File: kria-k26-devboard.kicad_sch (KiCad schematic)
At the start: 6 parts

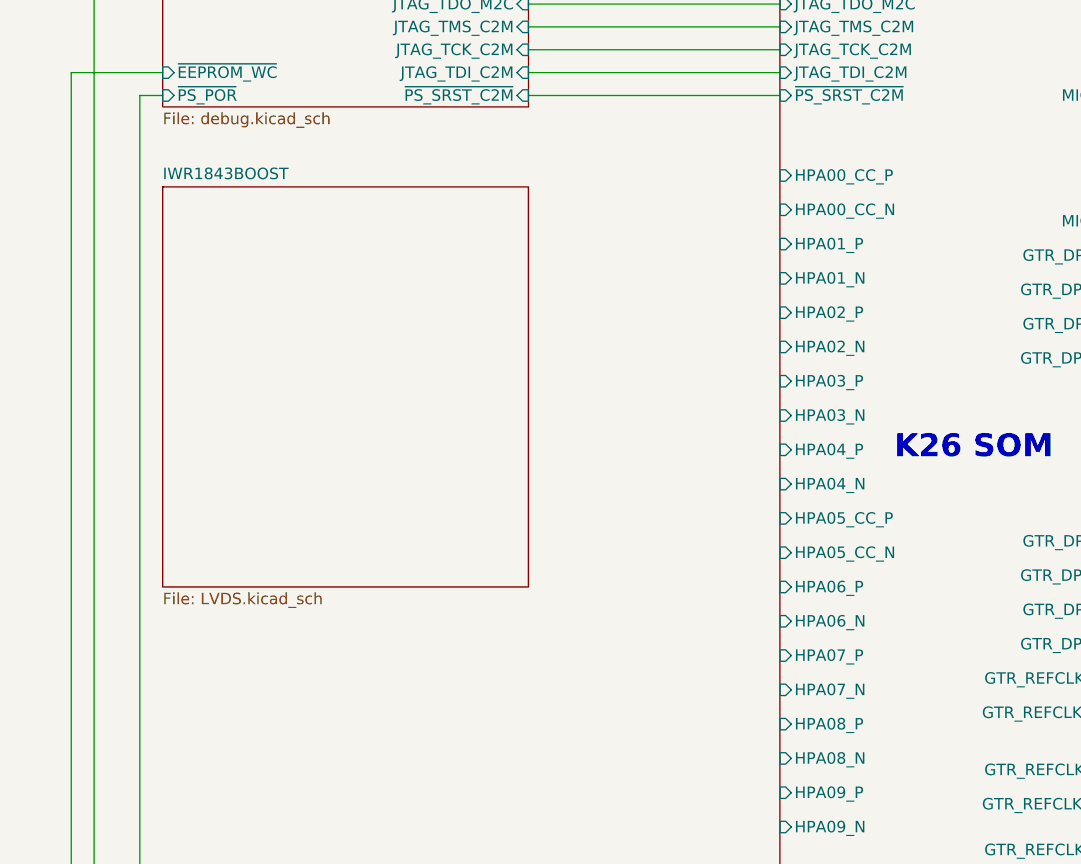
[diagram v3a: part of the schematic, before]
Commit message: Added all components and finished first attempt at schematic
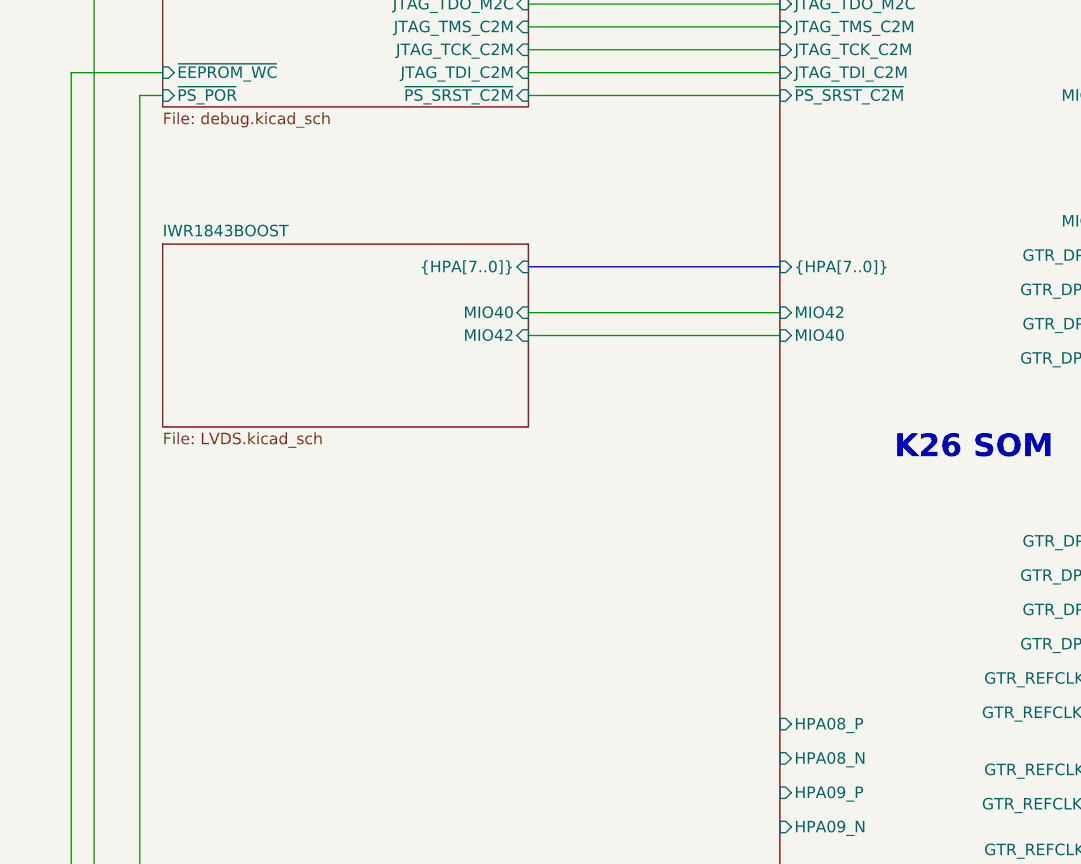
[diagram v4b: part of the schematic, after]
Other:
- sheet IWR1843BOOST ports: added MIO40, MIO42, {HPA[7..0]}; removed none
- sheet Xilinx K26 SOM ports: added MIO40, MIO42, {HPA[7..0]}; removed HPA00_CC_N, HPA00_CC_P, HPA01_N, HPA01_P, HPA02_N, HPA02_P, HPA03_N, HPA03_P, HPA04_N, HPA04_P, HPA05_CC_N, HPA05_CC_P, HPA06_N, HPA06_P, HPA07_N, HPA07_P
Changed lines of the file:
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@@
 		(comment 2 "Antmicro Ltd.")
 	)
+	(bus_alias "HPA[7..0]"
+		(members "HPA01_P" "HPA01_N" "HPA02_P" "HPA02_N" "HPA03_P" "HPA03_N" "HPA04_P"
+			"HPA04_N" "HPA00_CC_P" "HPA00_CC_N" "HPA05_CC_P" "HPA05_CC_N" "HPA06_P"
+			"HPA06_N" "HPA07_P" "HPA07_N"
+		)
+	)
 	(text "Logos"
 		(exclude_from_sim no)
@@
 		)
 	)
+	(wire
+		(pts
+			(xy 151.13 104.14) (xy 179.07 104.14)
+		)
+		(stroke
+			(width 0)
+			(type default)
+		)
+	)
 	(bus
 		(pts
@@
 		)
 	)
+	(bus
+		(pts
+			(xy 151.13 99.06) (xy 179.07 99.06)
+		)
+		(stroke
+			(width 0)
+			(type default)
+		)
+	)
 	(wire
 		(pts
@@
 	(wire
 		(pts
+			(xy 151.13 106.68) (xy 179.07 106.68)
+		)
+		(stroke
+			(width 0)
+			(type default)
+		)
+	)
+	(wire
+		(pts
 			(xy 233.68 184.15) (xy 248.92 184.15)
 		)
@@
 			)
 		)
-		(pin "HPA00_CC_P" input
-			(at 179.07 88.9 180)
-			(effects
-				(font
-					(size 1.27 1.27)
-				)
-				(justify left)
-			)
-		)
-		(pin "HPA00_CC_N" input
-			(at 179.07 92.71 180)
-			(effects
-				(font
-					(size 1.27 1.27)
-				)
-				(justify left)
-			)
-		)
-		(pin "HPA03_P" input
-			(at 179.07 111.76 180)
-			(effects
-				(font
-					(size 1.27 1.27)
-				)
-				(justify left)
-			)
-		)
-		(pin "HPA03_N" input
-			(at 179.07 115.57 180)
-			(effects
-				(font
-					(size 1.27 1.27)
-				)
-				(justify left)
-			)
-		)
 		(pin "HPA08_P" input
 			(at 179.07 149.86 180)
@@
 			)
 		)
-		(pin "HPA02_P" input
-			(at 179.07 104.14 180)
-			(effects
-				(font
-					(size 1.27 1.27)
-				)
-				(justify left)
-			)
-		)
-		(pin "HPA02_N" input
-			(at 179.07 107.95 180)
-			(effects
-				(font
-					(size 1.27 1.27)
-				)
-				(justify left)
-			)
-		)
-		(pin "HPA01_P" input
-			(at 179.07 96.52 180)
-			(effects
-				(font
-					(size 1.27 1.27)
-				)
-				(justify left)
-			)
-		)
-		(pin "HPA01_N" input
-			(at 179.07 100.33 180)
-			(effects
-				(font
-					(size 1.27 1.27)
-				)
-				(justify left)
-			)
-		)
 		(pin "HPA09_P" input
 			(at 179.07 157.48 180)
@@
 			)
 		)
-		(pin "HPA05_CC_P" input
-			(at 179.07 127 180)
-			(effects
-				(font
-					(size 1.27 1.27)
-				)
-				(justify left)
-			)
-		)
-		(pin "HPA05_CC_N" input
-			(at 179.07 130.81 180)
-			(effects
-				(font
-					(size 1.27 1.27)
-				)
-				(justify left)
-			)
-		)
-		(pin "HPA06_P" input
-			(at 179.07 134.62 180)
-			(effects
-				(font
-					(size 1.27 1.27)
-				)
-				(justify left)
-			)
-		)
-		(pin "HPA06_N" input
-			(at 179.07 138.43 180)
-			(effects
-				(font
-					(size 1.27 1.27)
-				)
-				(justify left)
-			)
-		)
-		(pin "HPA04_P" input
-			(at 179.07 119.38 180)
-			(effects
-				(font
-					(size 1.27 1.27)
-				)
-				(justify left)
-			)
-		)
-		(pin "HPA04_N" input
-			(at 179.07 123.19 180)
-			(effects
-				(font
-					(size 1.27 1.27)
-				)
-				(justify left)
-			)
-		)
-		(pin "HPA07_P" input
-			(at 179.07 142.24 180)
-			(effects
-				(font
-					(size 1.27 1.27)
-				)
-				(justify left)
-			)
-		)
-		(pin "HPA07_N" input
-			(at 179.07 146.05 180)
-			(effects
-				(font
-					(size 1.27 1.27)
-				)
-				(justify left)
-			)
-		)
 		(pin "HDA00_C" input
 			(at 179.07 168.91 180)
@@
 			)
 		)
+		(pin "MIO42" input
+			(at 179.07 104.14 180)
+			(effects
+				(font
+					(size 1.27 1.27)
+				)
+				(justify left)
+			)
+		)
+		(pin "MIO40" input
+			(at 179.07 106.68 180)
+			(effects
+				(font
+					(size 1.27 1.27)
+				)
+				(justify left)
+			)
+		)
+		(pin "{HPA[7..0]}" input
+			(at 179.07 99.06 180)
+			(effects
+				(font
+					(size 1.27 1.27)
+				)
+				(justify left)
+			)
+		)
 		(instances
 			(project "kria-k26-devboard"
@@
 	)
 	(sheet
-		(at 110.49 90.17)
-		(size 40.64 44.45)
+		(at 110.49 96.52)
+		(size 40.64 20.32)
 		(exclude_from_sim no)
 		(in_bom yes)
@@
 		)
 		(property "Sheetname" "IWR1843BOOST"
-			(at 110.49 89.4584 0)
+			(at 110.49 95.8084 0)
 			(effects
 				(font
@@
 		)
 		(property "Sheetfile" "LVDS.kicad_sch"
-			(at 110.49 135.2046 0)
+			(at 110.49 117.4246 0)
 			(effects
 				(font
@@
 			)
 		)
+		(pin "MIO40" input
+			(at 151.13 104.14 0)
+			(effects
+				(font
+					(size 1.27 1.27)
+				)
+				(justify right)
+			)
+		)
+		(pin "MIO42" input
+			(at 151.13 106.68 0)
+			(effects
+				(font
+					(size 1.27 1.27)
+				)
+				(justify right)
+			)
+		)
+		(pin "{HPA[7..0]}" input
+			(at 151.13 99.06 0)
+			(effects
+				(font
+					(size 1.27 1.27)
+				)
+				(justify right)
+			)
+		)

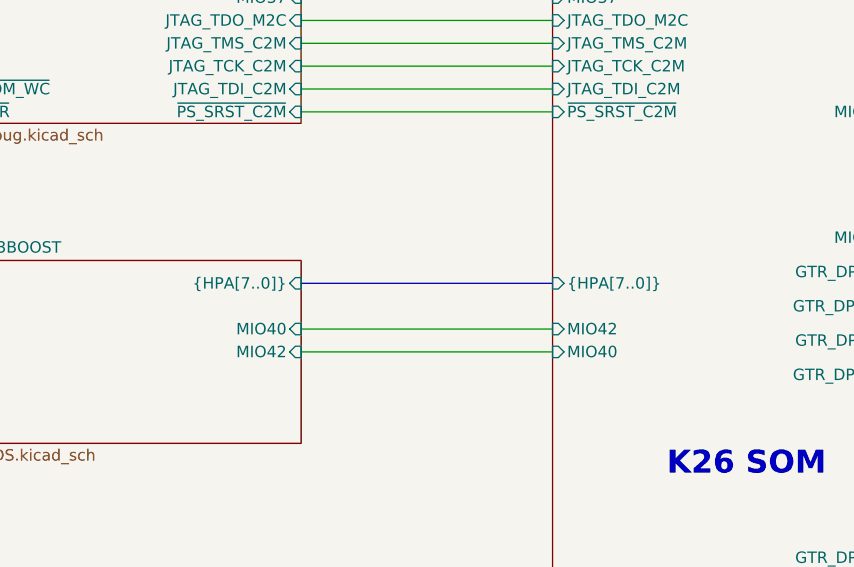
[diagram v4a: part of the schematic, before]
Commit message: Finished first set of LVDS signals
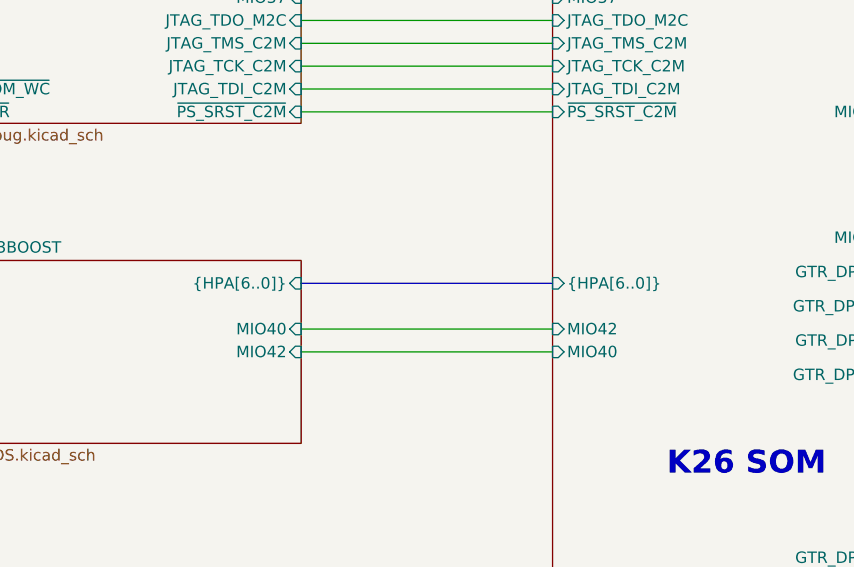
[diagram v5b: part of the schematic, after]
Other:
- sheet IWR1843BOOST ports: added {HPA[6..0]}; removed {HPA[7..0]}
- sheet Xilinx K26 SOM ports: added {HPA[6..0]}; removed {HPA[7..0]}
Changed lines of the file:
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@@
 		(comment 2 "Antmicro Ltd.")
 	)
-	(bus_alias "HPA[7..0]"
+	(bus_alias "HPA[6..0]"
 		(members "HPA01_P" "HPA01_N" "HPA02_P" "HPA02_N" "HPA03_P" "HPA03_N" "HPA04_P"
 			"HPA04_N" "HPA00_CC_P" "HPA00_CC_N" "HPA05_CC_P" "HPA05_CC_N" "HPA06_P"
-			"HPA06_N" "HPA07_P" "HPA07_N"
+			"HPA06_N"
 		)
 	)
@@
 			)
 		)
-		(pin "{HPA[7..0]}" input
+		(pin "{HPA[6..0]}" input
 			(at 179.07 99.06 180)
 			(effects
@@
 			)
 		)
-		(pin "{HPA[7..0]}" input
+		(pin "{HPA[6..0]}" input
 			(at 151.13 99.06 0)
 			(effects

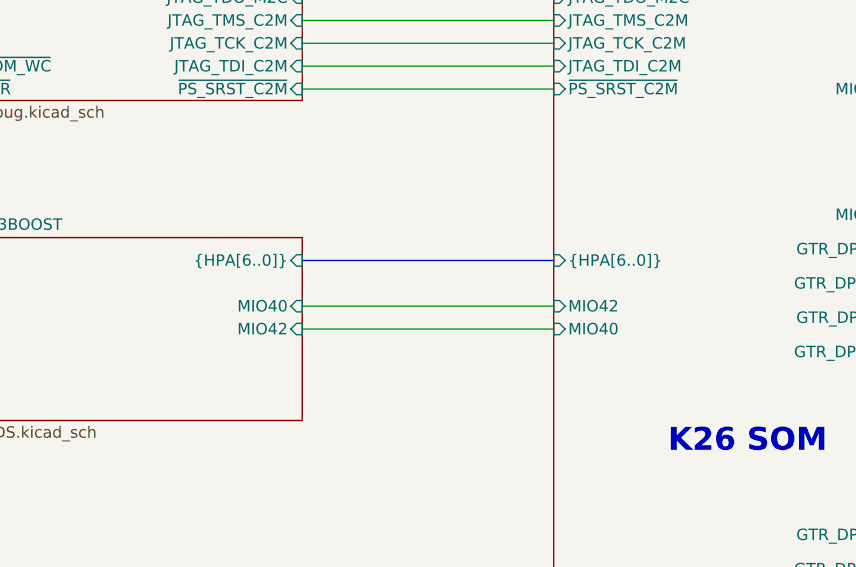
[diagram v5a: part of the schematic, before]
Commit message: Added second radar board connector, but haven't routed LVDS lines yet
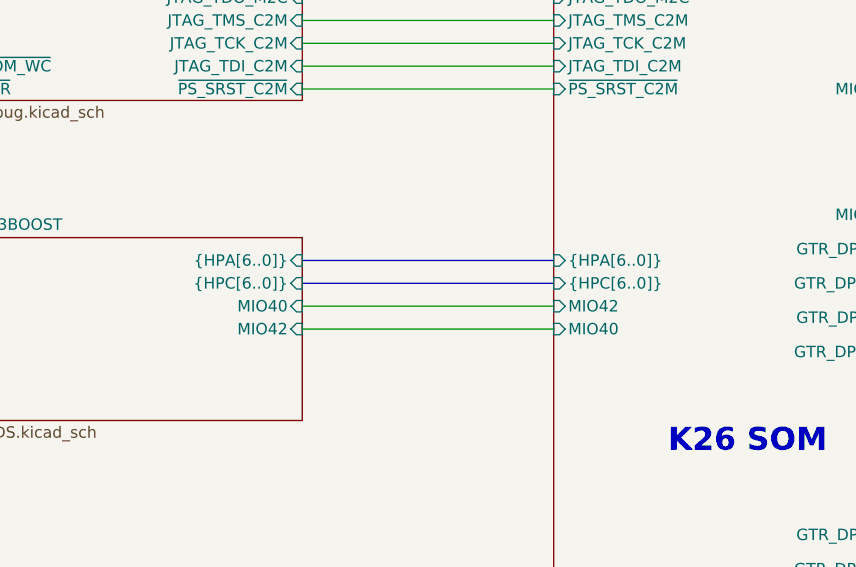
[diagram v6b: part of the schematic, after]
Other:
- sheet IWR1843BOOST ports: added {HPC[6..0]}; removed none
- sheet Xilinx K26 SOM ports: added {HPC[6..0]}; removed none
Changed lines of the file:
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@@
 		)
 	)
+	(bus
+		(pts
+			(xy 151.13 101.6) (xy 179.07 101.6)
+		)
+		(stroke
+			(width 0)
+			(type default)
+		)
+	)
 	(wire
 		(pts
@@
 			)
 		)
+		(pin "{HPC[6..0]}" input
+			(at 179.07 101.6 180)
+			(effects
+				(font
+					(size 1.27 1.27)
+				)
+				(justify left)
+			)
+		)
 		(instances
 			(project "kria-k26-devboard"
@@
 			(effects
 				(font
+					(size 1.27 1.27)
+				)
+				(justify right)
+			)
+		)
+		(pin "{HPC[6..0]}" input
+			(at 151.13 101.6 0)
+			(effects
+				(font

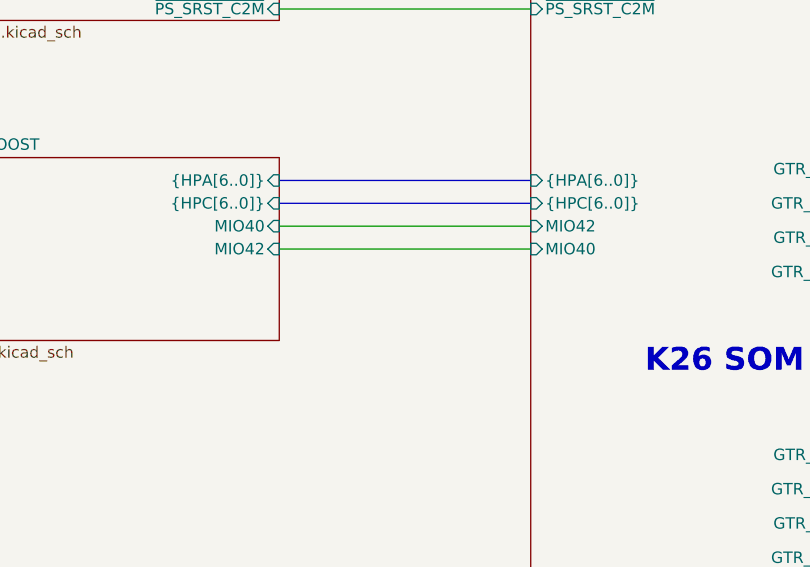
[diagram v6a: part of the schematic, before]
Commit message: Added second CAN interface, but haven't routed yet
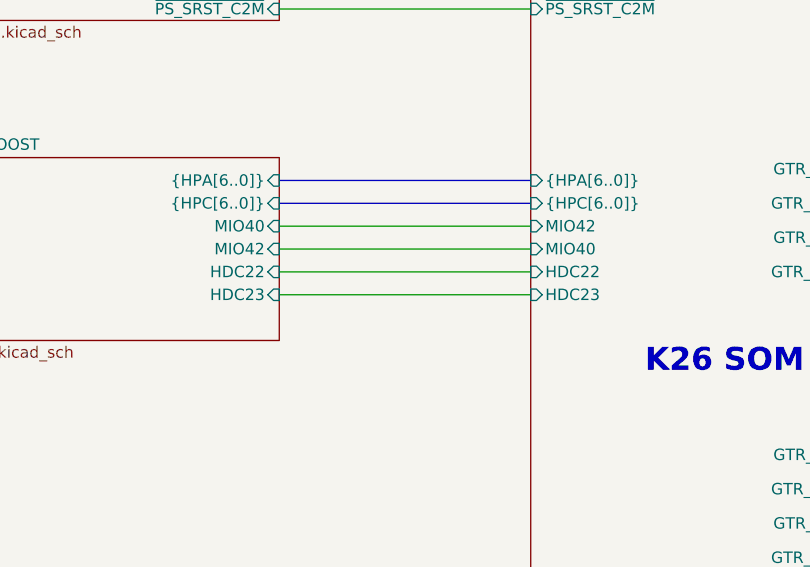
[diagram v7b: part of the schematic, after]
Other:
- sheet IWR1843BOOST ports: added HDC22, HDC23; removed none
- sheet Xilinx K26 SOM ports: added HDC22, HDC23; removed none
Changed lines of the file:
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@@
 	(wire
 		(pts
+			(xy 151.13 109.22) (xy 179.07 109.22)
+		)
+		(stroke
+			(width 0)
+			(type default)
+		)
+	)
+	(wire
+		(pts
 			(xy 171.45 228.6) (xy 171.45 241.3)
 		)
@@
 	(wire
 		(pts
+			(xy 151.13 111.76) (xy 179.07 111.76)
+		)
+		(stroke
+			(width 0)
+			(type default)
+		)
+	)
+	(wire
+		(pts
 			(xy 223.52 139.7) (xy 248.92 139.7)
 		)
@@
 			)
 		)
+		(pin "HDC22" input
+			(at 179.07 109.22 180)
+			(effects
+				(font
+					(size 1.27 1.27)
+				)
+				(justify left)
+			)
+		)
+		(pin "HDC23" input
+			(at 179.07 111.76 180)
+			(effects
+				(font
+					(size 1.27 1.27)
+				)
+				(justify left)
+			)
+		)
 		(instances
 			(project "kria-k26-devboard"
@@
 			(effects
 				(font
+					(size 1.27 1.27)
+				)
+				(justify right)
+			)
+		)
+		(pin "HDC22" input
+			(at 151.13 109.22 0)
+			(effects
+				(font
+					(size 1.27 1.27)
+				)
+				(justify right)
+			)
+		)
+		(pin "HDC23" input
+			(at 151.13 111.76 0)
+			(effects
+				(font
